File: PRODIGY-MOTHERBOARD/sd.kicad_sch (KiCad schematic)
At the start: 8 parts, among them J22 DM3BT-DSF-PEJS/C, Q1 DMP2045U-7, U4 IP4252CZ16

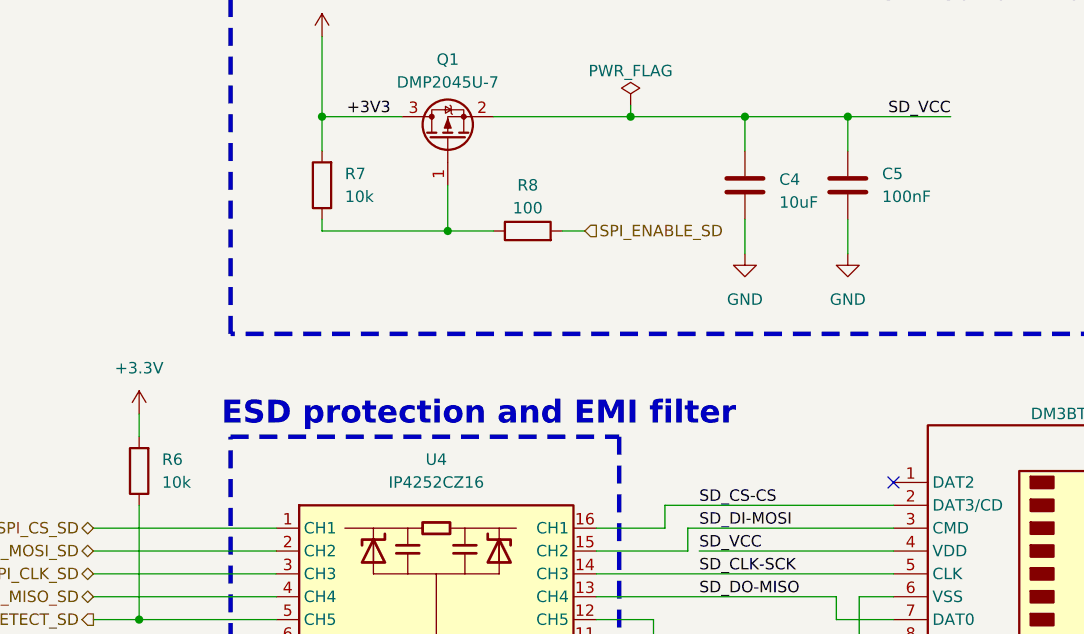
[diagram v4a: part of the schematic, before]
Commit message: SPI NFC schematic done.
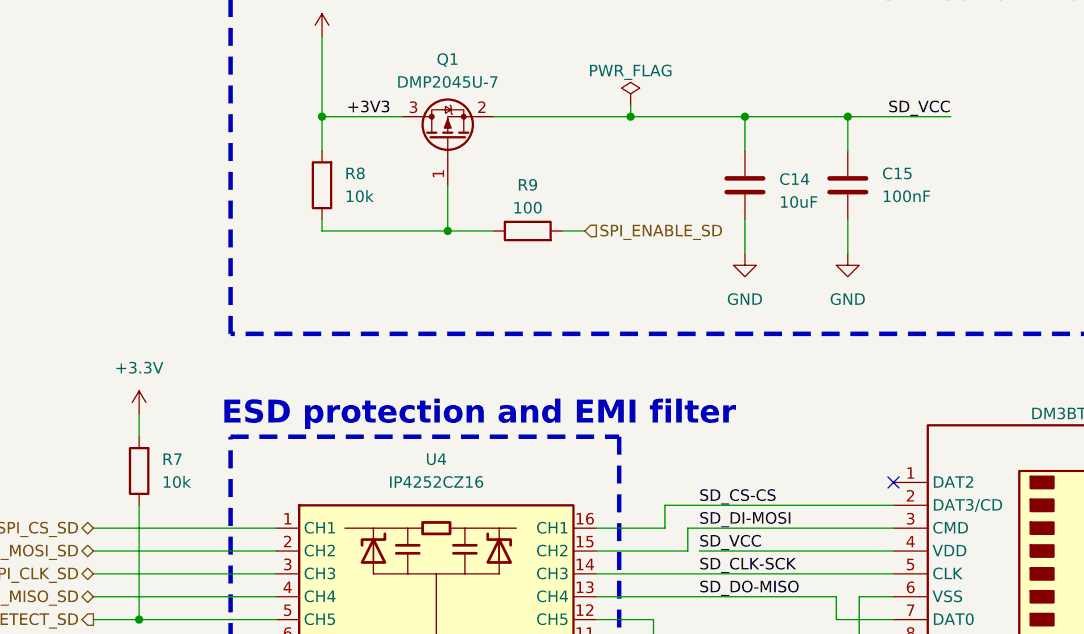
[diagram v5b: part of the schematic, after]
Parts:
- renumbered C4 to C14, C5 to C15, R6 to R7, R7 to R8, R8 to R9
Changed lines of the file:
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@@
 		(dnp no)
 		(fields_autoplaced yes)
-		(property "Reference" "#PWR021"
+		(property "Reference" "#PWR027"
 			(at 123.19 134.62 0)
 			(effects
@@
 			(project "PRODIGY-MOTHERBOARD"
 				(path "/f1c25860-8989-4190-bd24-2491d23ca7d9/e2913798-f444-47a6-8b64-53020d7d816b/c4f3c4b1-d676-4f7b-883c-6fdba835d106"
-					(reference "#PWR021")
+					(reference "#PWR027")
 					(unit 1)
 				)
@@
 		(dnp no)
 		(fields_autoplaced yes)
-		(property "Reference" "R8"
+		(property "Reference" "R9"
 			(at 133.35 66.04 90)
 			(effects
@@
 			(project "PRODIGY-MOTHERBOARD"
 				(path "/f1c25860-8989-4190-bd24-2491d23ca7d9/e2913798-f444-47a6-8b64-53020d7d816b/c4f3c4b1-d676-4f7b-883c-6fdba835d106"
-					(reference "R8")
+					(reference "R9")
 					(unit 1)
 				)
@@
 		(dnp no)
 		(fields_autoplaced yes)
-		(property "Reference" "R7"
+		(property "Reference" "R8"
 			(at 113.03 64.7699 0)
 			(effects
@@
 			(project "PRODIGY-MOTHERBOARD"
 				(path "/f1c25860-8989-4190-bd24-2491d23ca7d9/e2913798-f444-47a6-8b64-53020d7d816b/c4f3c4b1-d676-4f7b-883c-6fdba835d106"
-					(reference "R7")
+					(reference "R8")
 					(unit 1)
 				)
@@
 		(dnp no)
 		(fields_autoplaced yes)
-		(property "Reference" "#PWR020"
+		(property "Reference" "#PWR026"
 			(at 110.49 53.34 0)
 			(effects
@@
 			(project "PRODIGY-MOTHERBOARD"
 				(path "/f1c25860-8989-4190-bd24-2491d23ca7d9/e2913798-f444-47a6-8b64-53020d7d816b/c4f3c4b1-d676-4f7b-883c-6fdba835d106"
-					(reference "#PWR020")
+					(reference "#PWR026")
 					(unit 1)
 				)
@@
 		(dnp no)
 		(fields_autoplaced yes)
-		(property "Reference" "#PWR019"
+		(property "Reference" "#PWR025"
 			(at 90.17 95.25 0)
 			(effects
@@
 			(project "PRODIGY-MOTHERBOARD"
 				(path "/f1c25860-8989-4190-bd24-2491d23ca7d9/e2913798-f444-47a6-8b64-53020d7d816b/c4f3c4b1-d676-4f7b-883c-6fdba835d106"
-					(reference "#PWR019")
+					(reference "#PWR025")
 					(unit 1)
 				)
@@
 		(dnp no)
 		(fields_autoplaced yes)
-		(property "Reference" "#PWR023"
+		(property "Reference" "#PWR029"
 			(at 168.91 80.01 0)
 			(effects
@@
 			(project "PRODIGY-MOTHERBOARD"
 				(path "/f1c25860-8989-4190-bd24-2491d23ca7d9/e2913798-f444-47a6-8b64-53020d7d816b/c4f3c4b1-d676-4f7b-883c-6fdba835d106"
-					(reference "#PWR023")
+					(reference "#PWR029")
 					(unit 1)
 				)
@@
 		(dnp no)
 		(fields_autoplaced yes)
-		(property "Reference" "#PWR024"
+		(property "Reference" "#PWR030"
 			(at 170.18 134.62 0)
 			(effects
@@
 			(project "PRODIGY-MOTHERBOARD"
 				(path "/f1c25860-8989-4190-bd24-2491d23ca7d9/e2913798-f444-47a6-8b64-53020d7d816b/c4f3c4b1-d676-4f7b-883c-6fdba835d106"
-					(reference "#PWR024")
+					(reference "#PWR030")
 					(unit 1)
 				)
@@
 		(dnp no)
 		(fields_autoplaced yes)
-		(property "Reference" "C4"
+		(property "Reference" "C14"
 			(at 161.29 65.405 0)
 			(effects
@@
 			(project "PRODIGY-MOTHERBOARD"
 				(path "/f1c25860-8989-4190-bd24-2491d23ca7d9/e2913798-f444-47a6-8b64-53020d7d816b/c4f3c4b1-d676-4f7b-883c-6fdba835d106"
-					(reference "C4")
+					(reference "C14")
 					(unit 1)
 				)
@@
 		(dnp no)
 		(fields_autoplaced yes)
-		(property "Reference" "#PWR022"
+		(property "Reference" "#PWR028"
 			(at 157.48 80.01 0)
 			(effects
@@
 			(project "PRODIGY-MOTHERBOARD"
 				(path "/f1c25860-8989-4190-bd24-2491d23ca7d9/e2913798-f444-47a6-8b64-53020d7d816b/c4f3c4b1-d676-4f7b-883c-6fdba835d106"
-					(reference "#PWR022")
+					(reference "#PWR028")
 					(unit 1)
 				)
@@
 		(dnp no)
 		(fields_autoplaced yes)
-		(property "Reference" "R6"
+		(property "Reference" "R7"
 			(at 92.71 96.5199 0)
 			(effects
@@
 			(project "PRODIGY-MOTHERBOARD"
 				(path "/f1c25860-8989-4190-bd24-2491d23ca7d9/e2913798-f444-47a6-8b64-53020d7d816b/c4f3c4b1-d676-4f7b-883c-6fdba835d106"
-					(reference "R6")
+					(reference "R7")
 					(unit 1)
 				)
@@
 		(dnp no)
 		(fields_autoplaced yes)
-		(property "Reference" "C5"
+		(property "Reference" "C15"
 			(at 172.72 64.7699 0)
 			(effects
@@
 			(project "PRODIGY-MOTHERBOARD"
 				(path "/f1c25860-8989-4190-bd24-2491d23ca7d9/e2913798-f444-47a6-8b64-53020d7d816b/c4f3c4b1-d676-4f7b-883c-6fdba835d106"
-					(reference "C5")
-					(unit 1)
-				)
+					(reference "C15")
+					(unit 1)
+				)

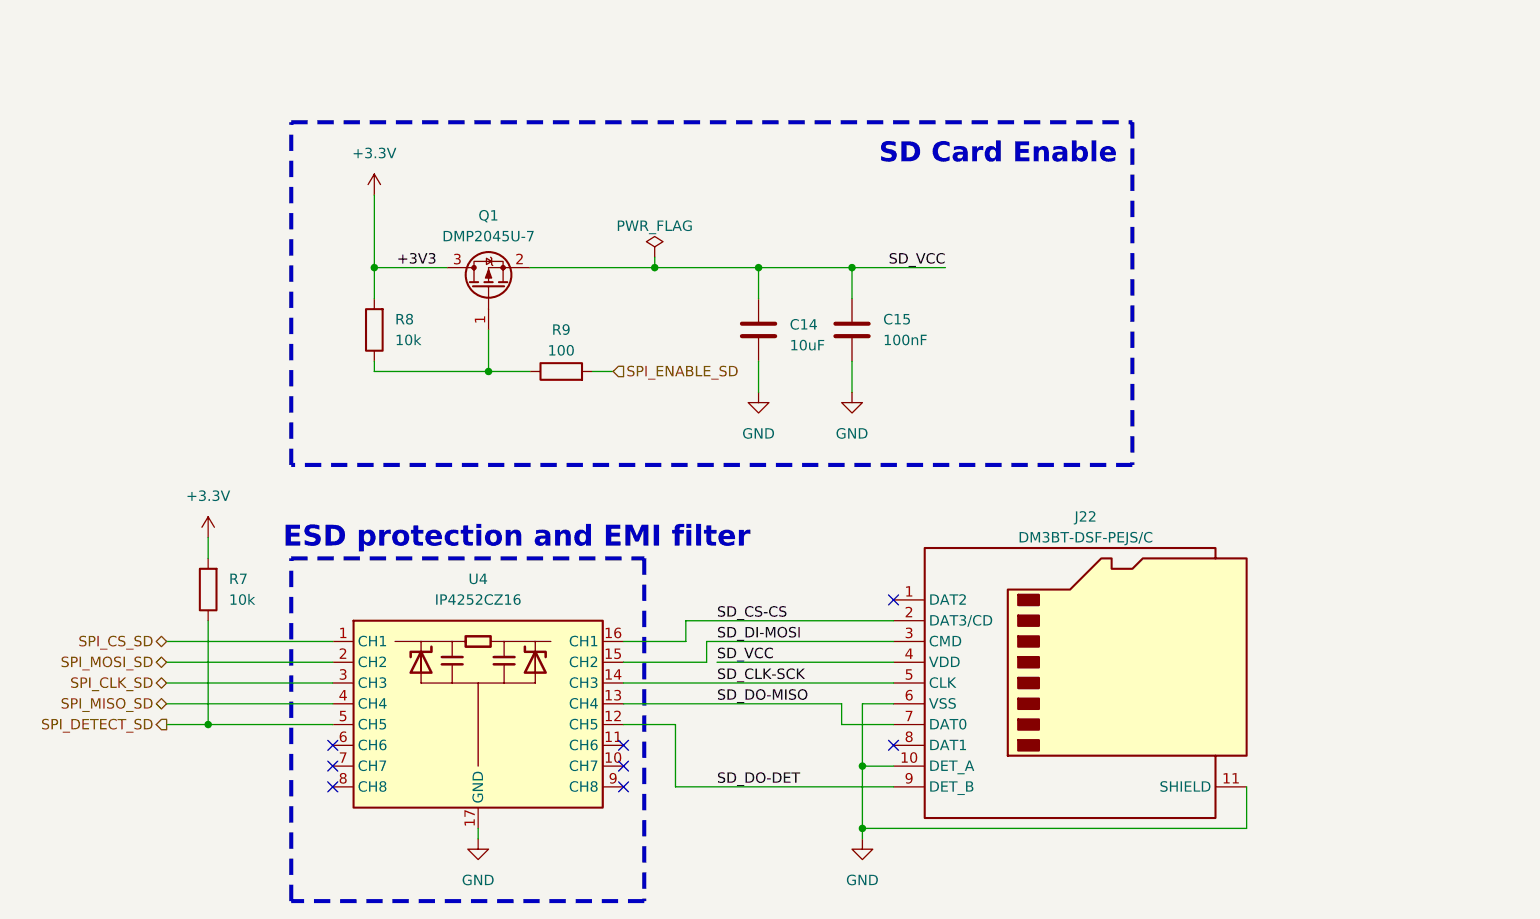
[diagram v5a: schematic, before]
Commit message: Added proper debounce filter elements to buttons.
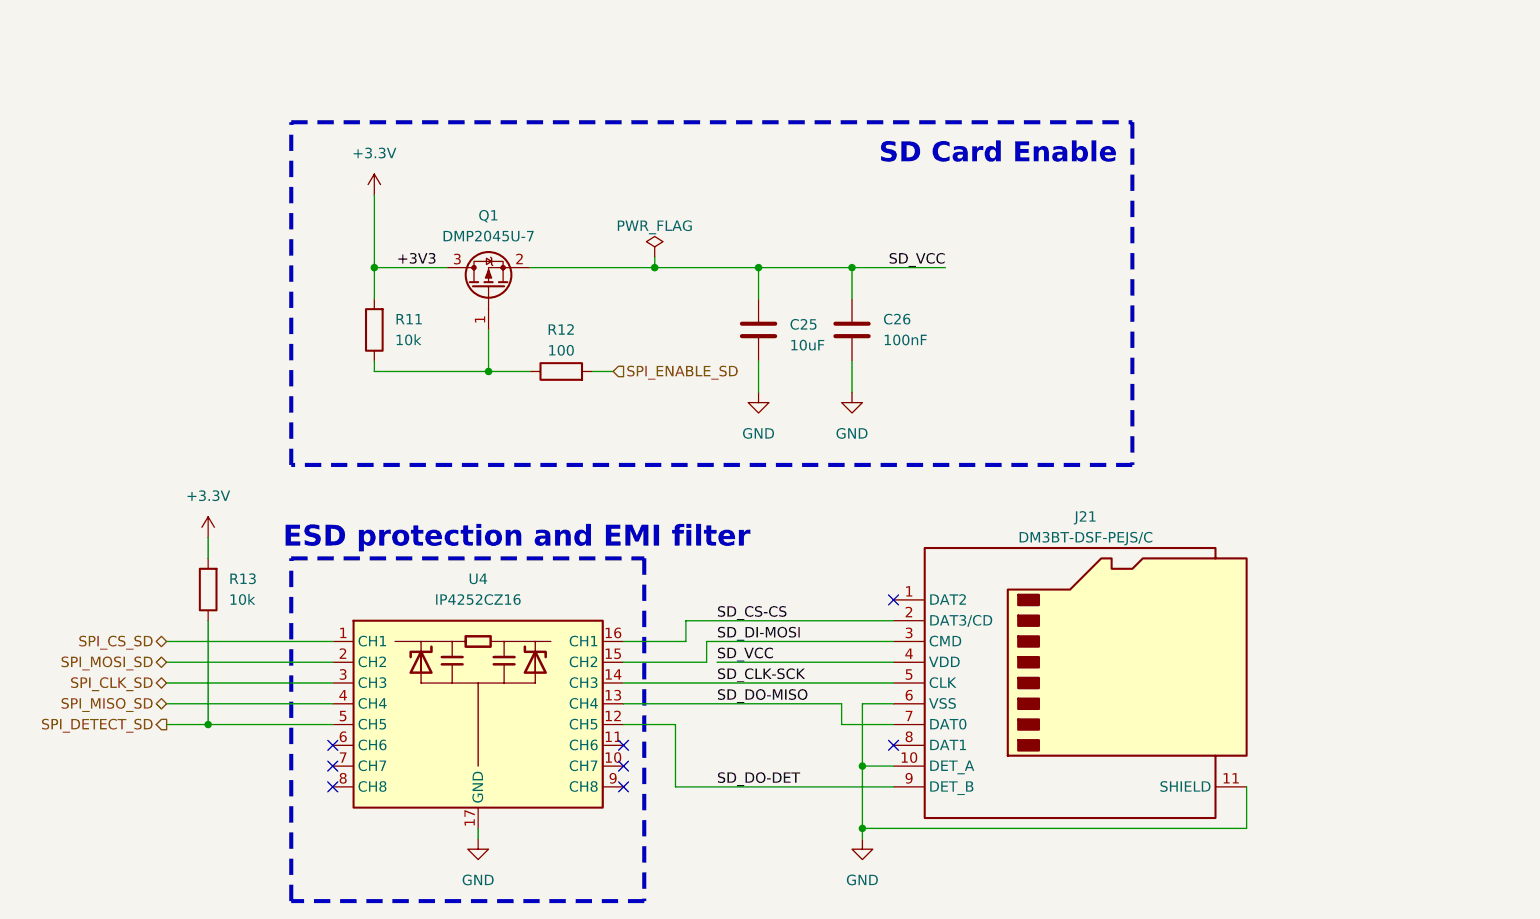
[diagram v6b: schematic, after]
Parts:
- renumbered C14 to C25, C15 to C26, J22 to J21, R8 to R11, R9 to R12, R7 to R13
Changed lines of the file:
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@@
 		(dnp no)
 		(fields_autoplaced yes)
-		(property "Reference" "#PWR027"
+		(property "Reference" "#PWR040"
 			(at 123.19 134.62 0)
 			(effects
@@
 			(project "PRODIGY-MOTHERBOARD"
 				(path "/f1c25860-8989-4190-bd24-2491d23ca7d9/e2913798-f444-47a6-8b64-53020d7d816b/c4f3c4b1-d676-4f7b-883c-6fdba835d106"
-					(reference "#PWR027")
+					(reference "#PWR040")
 					(unit 1)
 				)
@@
 		(dnp no)
 		(fields_autoplaced yes)
-		(property "Reference" "R9"
+		(property "Reference" "R12"
 			(at 133.35 66.04 90)
 			(effects
@@
 			(project "PRODIGY-MOTHERBOARD"
 				(path "/f1c25860-8989-4190-bd24-2491d23ca7d9/e2913798-f444-47a6-8b64-53020d7d816b/c4f3c4b1-d676-4f7b-883c-6fdba835d106"
-					(reference "R9")
+					(reference "R12")
 					(unit 1)
 				)
@@
 		(dnp no)
 		(fields_autoplaced yes)
-		(property "Reference" "R8"
+		(property "Reference" "R11"
 			(at 113.03 64.7699 0)
 			(effects
@@
 			(project "PRODIGY-MOTHERBOARD"
 				(path "/f1c25860-8989-4190-bd24-2491d23ca7d9/e2913798-f444-47a6-8b64-53020d7d816b/c4f3c4b1-d676-4f7b-883c-6fdba835d106"
-					(reference "R8")
+					(reference "R11")
 					(unit 1)
 				)
@@
 		(dnp no)
 		(fields_autoplaced yes)
-		(property "Reference" "#PWR026"
+		(property "Reference" "#PWR036"
 			(at 110.49 53.34 0)
 			(effects
@@
 			(project "PRODIGY-MOTHERBOARD"
 				(path "/f1c25860-8989-4190-bd24-2491d23ca7d9/e2913798-f444-47a6-8b64-53020d7d816b/c4f3c4b1-d676-4f7b-883c-6fdba835d106"
-					(reference "#PWR026")
+					(reference "#PWR036")
 					(unit 1)
 				)
@@
 		(dnp no)
 		(fields_autoplaced yes)
-		(property "Reference" "#PWR025"
+		(property "Reference" "#PWR039"
 			(at 90.17 95.25 0)
 			(effects
@@
 			(project "PRODIGY-MOTHERBOARD"
 				(path "/f1c25860-8989-4190-bd24-2491d23ca7d9/e2913798-f444-47a6-8b64-53020d7d816b/c4f3c4b1-d676-4f7b-883c-6fdba835d106"
-					(reference "#PWR025")
+					(reference "#PWR039")
 					(unit 1)
 				)
@@
 		(dnp no)
 		(fields_autoplaced yes)
-		(property "Reference" "#PWR029"
+		(property "Reference" "#PWR038"
 			(at 168.91 80.01 0)
 			(effects
@@
 			(project "PRODIGY-MOTHERBOARD"
 				(path "/f1c25860-8989-4190-bd24-2491d23ca7d9/e2913798-f444-47a6-8b64-53020d7d816b/c4f3c4b1-d676-4f7b-883c-6fdba835d106"
-					(reference "#PWR029")
+					(reference "#PWR038")
 					(unit 1)
 				)
@@
 		(dnp no)
 		(fields_autoplaced yes)
-		(property "Reference" "#PWR030"
+		(property "Reference" "#PWR041"
 			(at 170.18 134.62 0)
 			(effects
@@
 			(project "PRODIGY-MOTHERBOARD"
 				(path "/f1c25860-8989-4190-bd24-2491d23ca7d9/e2913798-f444-47a6-8b64-53020d7d816b/c4f3c4b1-d676-4f7b-883c-6fdba835d106"
-					(reference "#PWR030")
+					(reference "#PWR041")
 					(unit 1)
 				)
@@
 		(dnp no)
 		(fields_autoplaced yes)
-		(property "Reference" "C14"
+		(property "Reference" "C25"
 			(at 161.29 65.405 0)
 			(effects
@@
 			(project "PRODIGY-MOTHERBOARD"
 				(path "/f1c25860-8989-4190-bd24-2491d23ca7d9/e2913798-f444-47a6-8b64-53020d7d816b/c4f3c4b1-d676-4f7b-883c-6fdba835d106"
-					(reference "C14")
+					(reference "C25")
 					(unit 1)
 				)
@@
 		(dnp no)
 		(fields_autoplaced yes)
-		(property "Reference" "#PWR028"
+		(property "Reference" "#PWR037"
 			(at 157.48 80.01 0)
 			(effects
@@
 			(project "PRODIGY-MOTHERBOARD"
 				(path "/f1c25860-8989-4190-bd24-2491d23ca7d9/e2913798-f444-47a6-8b64-53020d7d816b/c4f3c4b1-d676-4f7b-883c-6fdba835d106"
-					(reference "#PWR028")
+					(reference "#PWR037")
 					(unit 1)
 				)
@@
 		(dnp no)
 		(fields_autoplaced yes)
-		(property "Reference" "R7"
+		(property "Reference" "R13"
 			(at 92.71 96.5199 0)
 			(effects
@@
 			(project "PRODIGY-MOTHERBOARD"
 				(path "/f1c25860-8989-4190-bd24-2491d23ca7d9/e2913798-f444-47a6-8b64-53020d7d816b/c4f3c4b1-d676-4f7b-883c-6fdba835d106"
-					(reference "R7")
+					(reference "R13")
 					(unit 1)
 				)
@@
 		(dnp no)
 		(fields_autoplaced yes)
-		(property "Reference" "C15"
+		(property "Reference" "C26"
 			(at 172.72 64.7699 0)
 			(effects
@@
 			(project "PRODIGY-MOTHERBOARD"
 				(path "/f1c25860-8989-4190-bd24-2491d23ca7d9/e2913798-f444-47a6-8b64-53020d7d816b/c4f3c4b1-d676-4f7b-883c-6fdba835d106"
-					(reference "C15")
+					(reference "C26")
 					(unit 1)
 				)
@@
 		(on_board yes)
 		(dnp no)
-		(property "Reference" "J22"
+		(property "Reference" "J21"
 			(at 197.485 88.9 0)
 			(effects
@@
 			(project "PRODIGY-MOTHERBOARD"
 				(path "/f1c25860-8989-4190-bd24-2491d23ca7d9/e2913798-f444-47a6-8b64-53020d7d816b/c4f3c4b1-d676-4f7b-883c-6fdba835d106"
-					(reference "J22")
-					(unit 1)
-				)
+					(reference "J21")
+					(unit 1)
+				)
